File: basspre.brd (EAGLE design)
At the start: 37.5 x 28.7 mm, 26 parts, among them U101 TLE2426IDR, U102 LF351D, U103 LM4250

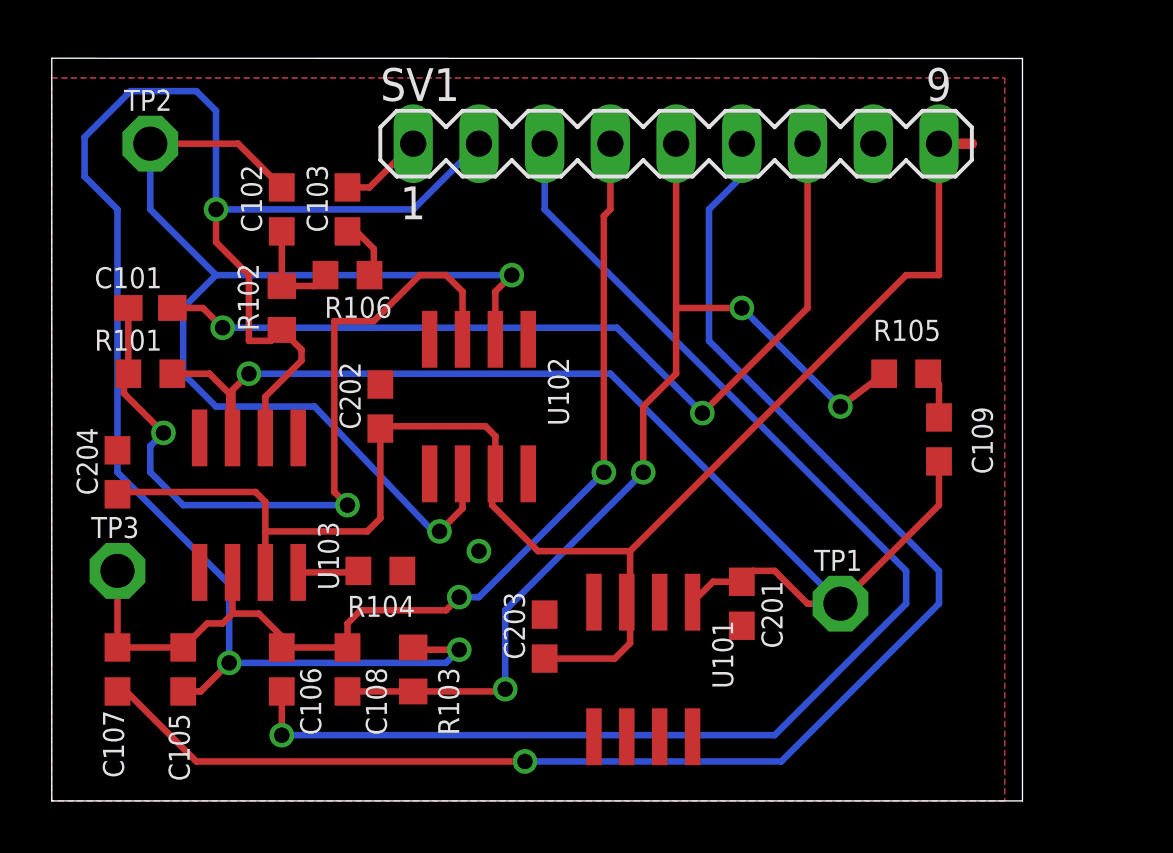
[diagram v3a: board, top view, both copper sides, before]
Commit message: switched to 10 pin system so bass pot can be three terminal in future revisions without changing connection.
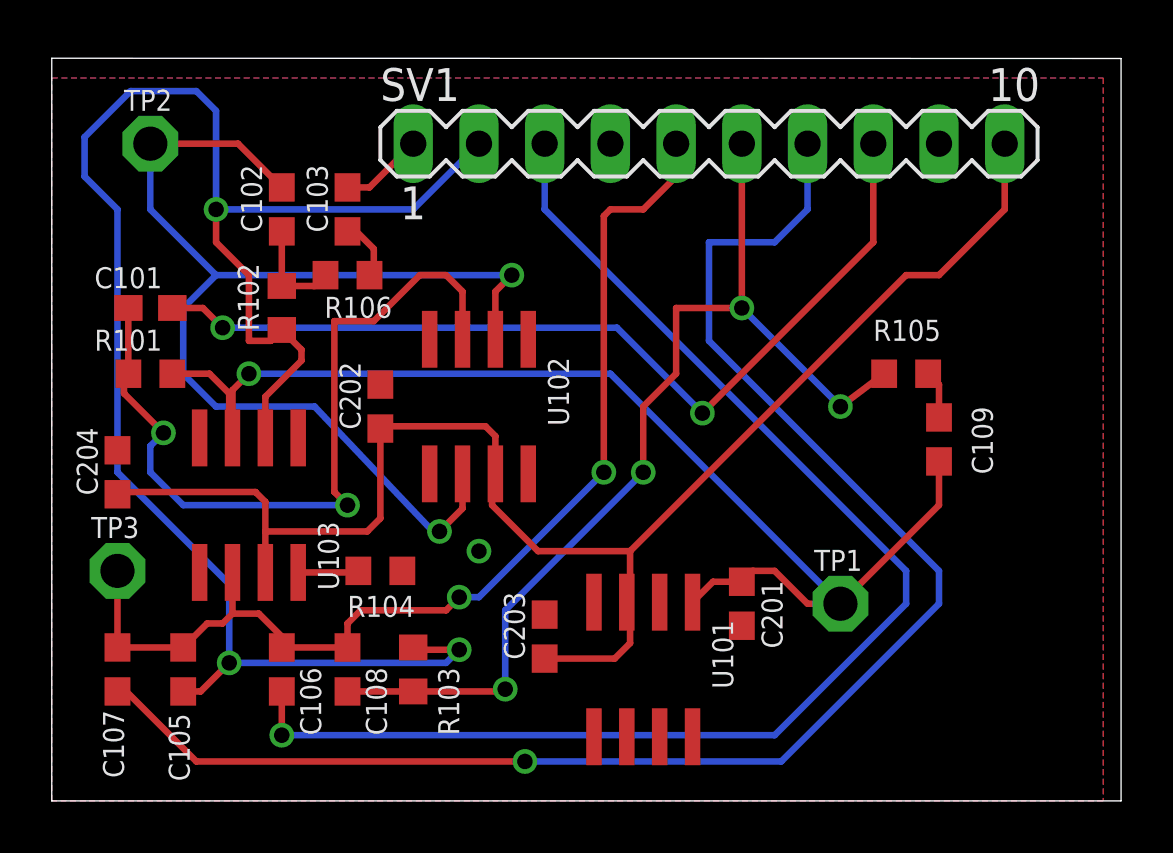
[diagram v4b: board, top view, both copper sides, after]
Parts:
- SV1: device con-lstb:MA09-1 -> con-lstb:MA10-1
- moved SV1 1.27 mm to (25.4, 25.4)
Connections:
- new net BASS3: SV1.4
- net BASS1: now also SV1.6; no longer SV1.5
- net BASS2: now also SV1.5; no longer SV1.4
- net GND: now also SV1.9; no longer SV1.8
- net INPUT: now also SV1.8; no longer SV1.7
- net OUTPUT: now also SV1.7; no longer SV1.6
- net V+: now also SV1.10; no longer SV1.9
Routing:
- net OUTPUT: track 57.4 -> 59.9 mm
- net BASS2: track 40.8 -> 42.6 mm
- net INPUT: track 34.3 -> 35.3 mm
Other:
- board size 37.5 x 28.7 mm -> 41.3 x 28.7 mm
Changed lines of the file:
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@@
 <board>
 <plain>
-<wire x1="0" y1="0" x2="37.516" y2="0" width="0" layer="20"/>
-<wire x1="37.516" y1="0" x2="37.516" y2="28.692" width="0" layer="20"/>
-<wire x1="37.516" y1="28.692" x2="0" y2="28.702" width="0" layer="20"/>
+<wire x1="0" y1="0" x2="41.326" y2="0" width="0" layer="20"/>
+<wire x1="41.326" y1="0" x2="41.326" y2="28.692" width="0" layer="20"/>
+<wire x1="41.326" y1="28.692" x2="0" y2="28.702" width="0" layer="20"/>
 <wire x1="0" y1="28.702" x2="0" y2="0" width="0" layer="20"/>
 <text x="35.56" y="17.78" size="1.6764" layer="22" font="vector" rot="MR0">BASSPRE-MM2
@@
 <attribute name="VALUE" x="4.572" y="11.811" size="1.27" layer="27" rot="R90"/>
 </element>
-<element name="SV1" library="con-lstb" package="MA09-1" value="" x="24.13" y="25.4">
-<attribute name="OC_NEWARK" value="unknown" x="49.53" y="8.89" size="1.778" layer="27" display="off"/>
-<attribute name="MPN" value="" x="49.53" y="8.89" size="1.778" layer="27" display="off"/>
-<attribute name="MF" value="" x="49.53" y="8.89" size="1.778" layer="27" display="off"/>
-<attribute name="OC_FARNELL" value="unknown" x="49.53" y="8.89" size="1.778" layer="27" display="off"/>
+<element name="SV1" library="con-lstb" package="MA10-1" value="" x="25.4" y="25.4">
+<attribute name="OC_NEWARK" value="unknown" x="50.8" y="8.89" size="1.778" layer="27" display="off"/>
+<attribute name="MPN" value="" x="50.8" y="8.89" size="1.778" layer="27" display="off"/>
+<attribute name="MF" value="" x="50.8" y="8.89" size="1.778" layer="27" display="off"/>
+<attribute name="OC_FARNELL" value="unknown" x="50.8" y="8.89" size="1.778" layer="27" display="off"/>
 </element>
 <element name="U$1" library="SparkFun" package="OSHW-LOGO-L" value="" x="32.766" y="12.7" rot="MR0"/>
@@
 <contactref element="U102" pad="4"/>
 <contactref element="U103" pad="4"/>
-<contactref element="SV1" pad="8"/>
 <contactref element="C204" pad="2"/>
 <contactref element="C201" pad="2"/>
@@
 <vertex x="0" y="0"/>
 <vertex x="0" y="27.94"/>
-<vertex x="36.83" y="27.94"/>
-<vertex x="36.83" y="0"/>
+<vertex x="40.64" y="27.94"/>
+<vertex x="40.64" y="0"/>
 </polygon>
 <polygon width="0.4064" layer="1">
 <vertex x="0" y="27.94"/>
-<vertex x="36.83" y="27.94"/>
-<vertex x="36.83" y="0"/>
+<vertex x="40.64" y="27.94"/>
+<vertex x="40.64" y="0"/>
 <vertex x="0" y="0"/>
 </polygon>
 <via x="16.51" y="9.652" extent="1-16" drill="0.6" shape="square"/>
+<contactref element="SV1" pad="9"/>
 </signal>
 <signal name="V+">
@@
 <contactref element="U103" pad="7"/>
 <contactref element="U102" pad="7"/>
-<contactref element="SV1" pad="9"/>
 <contactref element="C202" pad="1"/>
 <contactref element="C203" pad="1"/>
 <contactref element="C204" pad="1"/>
-<wire x1="34.29" y1="25.4" x2="35.56" y2="25.4" width="0.4064" layer="1"/>
-<wire x1="34.29" y1="25.4" x2="34.29" y2="20.32" width="0.254" layer="1"/>
 <wire x1="34.29" y1="20.32" x2="33.02" y2="20.32" width="0.254" layer="1"/>
 <wire x1="33.02" y1="20.32" x2="22.352" y2="9.652" width="0.254" layer="1"/>
@@
 <wire x1="12.7" y1="10.922" x2="12.192" y2="10.414" width="0.254" layer="1"/>
 <wire x1="12.192" y1="10.414" x2="8.255" y2="10.414" width="0.254" layer="1"/>
+<contactref element="SV1" pad="10"/>
+<wire x1="34.29" y1="20.32" x2="36.83" y2="22.86" width="0.254" layer="1"/>
+<wire x1="36.83" y1="22.86" x2="36.83" y2="25.4" width="0.254" layer="1"/>
 </signal>
 <signal name="N$2">
@@
 <signal name="INPUT">
 <contactref element="C101" pad="2"/>
-<contactref element="SV1" pad="7"/>
 <wire x1="4.66" y1="19.05" x2="5.842" y2="19.05" width="0.254" layer="1"/>
 <wire x1="5.842" y1="19.05" x2="6.604" y2="18.288" width="0.254" layer="1"/>
@@
 <wire x1="21.844" y1="18.288" x2="25.146" y2="14.986" width="0.254" layer="16"/>
 <via x="25.146" y="14.986" extent="1-16" drill="0.6" shape="square"/>
-<wire x1="25.146" y1="14.986" x2="29.21" y2="19.05" width="0.254" layer="1"/>
-<wire x1="29.21" y1="19.05" x2="29.21" y2="25.4" width="0.254" layer="1"/>
+<wire x1="25.146" y1="14.986" x2="31.75" y2="21.59" width="0.254" layer="1"/>
+<contactref element="SV1" pad="8"/>
+<wire x1="31.75" y1="21.59" x2="31.75" y2="25.4" width="0.254" layer="1"/>
 </signal>
 <signal name="BASS2">
@@
 <contactref element="C107" pad="2"/>
 <contactref element="TP3" pad="TP"/>
-<contactref element="SV1" pad="4"/>
 <wire x1="8.89" y1="5.93" x2="11.43" y2="5.93" width="0.254" layer="1"/>
 <wire x1="2.54" y1="5.93" x2="5.08" y2="5.93" width="0.254" layer="1"/>
@@
 <wire x1="21.336" y1="12.7" x2="21.336" y2="22.606" width="0.254" layer="1"/>
 <wire x1="21.336" y1="22.606" x2="21.59" y2="22.86" width="0.254" layer="1"/>
-<wire x1="21.59" y1="22.86" x2="21.59" y2="25.4" width="0.254" layer="1"/>
+<contactref element="SV1" pad="5"/>
+<wire x1="21.59" y1="22.86" x2="22.86" y2="22.86" width="0.254" layer="1"/>
+<wire x1="22.86" y1="22.86" x2="24.13" y2="24.13" width="0.254" layer="1"/>
+<wire x1="24.13" y1="24.13" x2="24.13" y2="25.4" width="0.254" layer="1"/>
 </signal>
 <signal name="TREBLE2">
@@
 <contactref element="R103" pad="2"/>
 <contactref element="C108" pad="2"/>
-<contactref element="SV1" pad="5"/>
 <wire x1="11.43" y1="4.23" x2="13.97" y2="4.23" width="0.254" layer="1"/>
 <wire x1="13.97" y1="4.23" x2="17.438" y2="4.23" width="0.254" layer="1"/>
@@
 <wire x1="24.13" y1="16.51" x2="24.13" y2="19.05" width="0.254" layer="1"/>
 <contactref element="R105" pad="1"/>
-<wire x1="24.13" y1="19.05" x2="24.13" y2="25.4" width="0.254" layer="1"/>
 <wire x1="32.17" y1="16.51" x2="30.48" y2="15.24" width="0.254" layer="1"/>
 <via x="30.48" y="15.24" extent="1-16" drill="0.6" shape="square"/>
@@
 <via x="26.67" y="19.05" extent="1-16" drill="0.6" shape="square"/>
 <wire x1="26.67" y1="19.05" x2="24.13" y2="19.05" width="0.254" layer="1"/>
+<contactref element="SV1" pad="6"/>
+<wire x1="26.67" y1="19.05" x2="26.67" y2="25.4" width="0.254" layer="1"/>
 </signal>
 <signal name="N$1">
@@
 </signal>
 <signal name="OUTPUT">
-<contactref element="SV1" pad="6"/>
 <contactref element="C107" pad="1"/>
 <wire x1="2.54" y1="4.23" x2="2.882" y2="4.23" width="0.254" layer="1"/>
@@
 <wire x1="34.29" y1="7.62" x2="34.29" y2="8.89" width="0.254" layer="16"/>
 <wire x1="34.29" y1="8.89" x2="25.4" y2="17.78" width="0.254" layer="16"/>
-<wire x1="25.4" y1="17.78" x2="25.4" y2="22.86" width="0.254" layer="16"/>
-<wire x1="25.4" y1="22.86" x2="26.67" y2="24.13" width="0.254" layer="16"/>
-<wire x1="26.67" y1="24.13" x2="26.67" y2="25.4" width="0.254" layer="16"/>
+<contactref element="SV1" pad="7"/>
+<wire x1="25.4" y1="17.78" x2="25.4" y2="21.59" width="0.254" layer="16"/>
+<wire x1="25.4" y1="21.59" x2="27.94" y2="21.59" width="0.254" layer="16"/>
+<wire x1="27.94" y1="21.59" x2="29.21" y2="22.86" width="0.254" layer="16"/>
+<wire x1="29.21" y1="22.86" x2="29.21" y2="25.4" width="0.254" layer="16"/>
 </signal>
 <signal name="N$4">
@@
 <wire x1="12.446" y1="20.486" x2="12.28" y2="20.32" width="0.254" layer="1"/>
 </signal>
+<signal name="BASS3">
+<contactref element="SV1" pad="4"/>
+</signal>
 </signals>

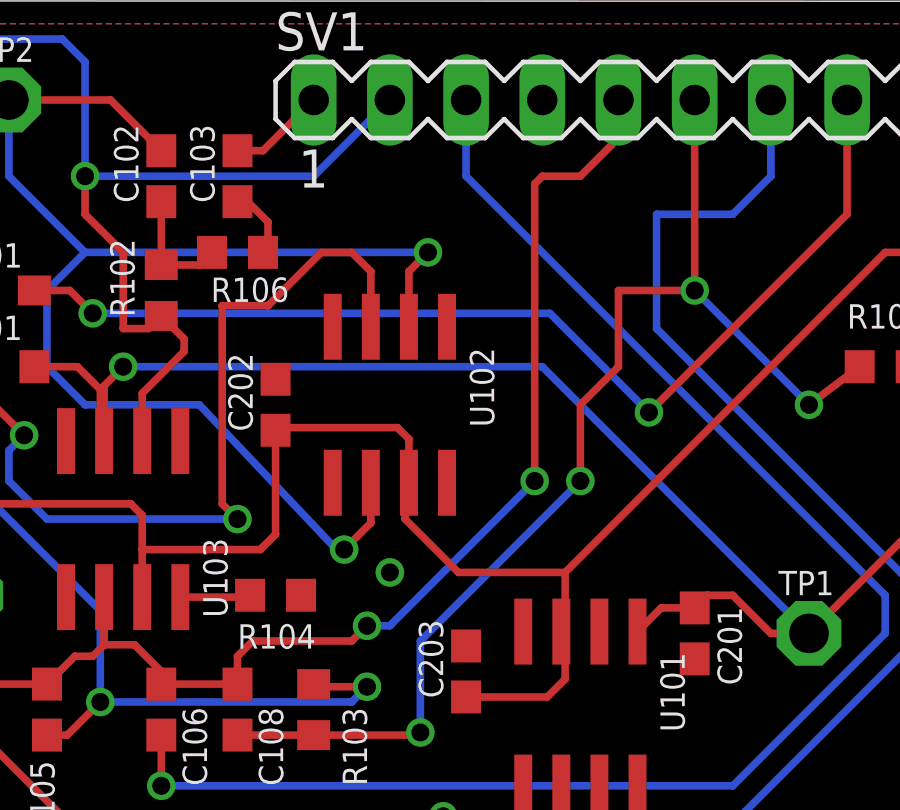
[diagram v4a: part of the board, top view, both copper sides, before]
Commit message: switched to two lm4250s for micropower operation, added readme
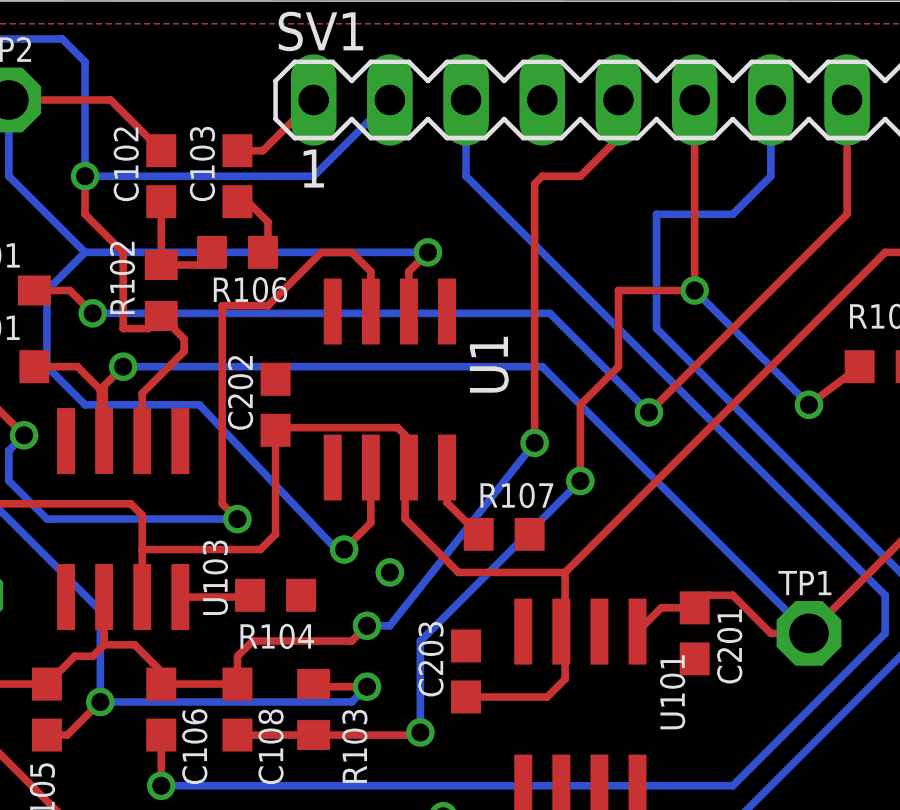
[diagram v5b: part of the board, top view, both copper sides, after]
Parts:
- removed U102: LF351D, linear:SO08
- added R107: 1.5M, resistor:R0603
- added U1: LM4250, russell_random:SOIC8
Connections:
- new net R107: R107.1, U1.8
- net C1: now also U1.3; no longer U102.3
- net GND: now also R107.2, U1.4; no longer U102.4
- net N$3: now also U1.2, U1.6; no longer U102.2, U102.6
- net V+: now also U1.7; no longer U102.7
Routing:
- net R107: track 0.00 -> 2.66 mm
- net C1: track 30.5 -> 30.0 mm
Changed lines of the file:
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@@
 <attribute name="VALUE" x="11.811" y="6.858" size="1.27" layer="27"/>
-</element>
-<element name="U102" library="linear" package="SO08" value="LF351D" x="16.51" y="15.24" smashed="yes" rot="R180">
-<attribute name="NAME" x="19.177" y="17.145" size="0.8128" layer="25" rot="R270"/>
-<attribute name="VALUE" x="12.573" y="17.145" size="1.27" layer="27" rot="R270"/>
 </element>
 <element name="C101" library="resistor" package="C0603" value="1uF" x="3.81" y="19.05" smashed="yes">
@@
 <attribute name="VALUE" x="10.541" y="18.288" size="1.27" layer="27"/>
 </element>
+<element name="U1" library="russell_random" package="SOIC8" value="LM4250" x="16.51" y="15.748" rot="R180"/>
+<element name="R107" library="resistor" package="R0603" value="1.5M" x="20.32" y="10.922" smashed="yes">
+<attribute name="NAME" x="19.431" y="11.811" size="0.8128" layer="25"/>
+<attribute name="VALUE" x="19.431" y="8.89" size="1.27" layer="27"/>
+</element>
 </elements>
 <signals>
@@
 <contactref element="U101" pad="2"/>
 <contactref element="R104" pad="2"/>
-<contactref element="U102" pad="4"/>
 <contactref element="U103" pad="4"/>
 <contactref element="C204" pad="2"/>
@@
 <via x="16.51" y="9.652" extent="1-16" drill="0.6" shape="square"/>
 <contactref element="SV1" pad="9"/>
+<contactref element="U1" pad="4"/>
+<contactref element="R107" pad="2"/>
 </signal>
 <signal name="V+">
 <contactref element="U101" pad="3"/>
 <contactref element="U103" pad="7"/>
-<contactref element="U102" pad="7"/>
 <contactref element="C202" pad="1"/>
 <contactref element="C203" pad="1"/>
@@
 <wire x1="22.352" y1="9.652" x2="18.796" y2="9.652" width="0.254" layer="1"/>
 <wire x1="18.796" y1="9.652" x2="17.018" y2="11.43" width="0.254" layer="1"/>
-<wire x1="17.018" y1="11.43" x2="17.018" y2="12.513" width="0.254" layer="1"/>
-<wire x1="17.018" y1="12.513" x2="17.145" y2="12.64" width="0.254" layer="1"/>
-<wire x1="17.145" y1="12.64" x2="17.145" y2="14.097" width="0.254" layer="1"/>
+<wire x1="17.018" y1="11.43" x2="17.018" y2="13.148" width="0.254" layer="1"/>
 <wire x1="17.145" y1="14.097" x2="16.764" y2="14.478" width="0.254" layer="1"/>
 <wire x1="16.764" y1="14.478" x2="12.788" y2="14.478" width="0.254" layer="1"/>
@@
 <wire x1="34.29" y1="20.32" x2="36.83" y2="22.86" width="0.254" layer="1"/>
 <wire x1="36.83" y1="22.86" x2="36.83" y2="25.4" width="0.254" layer="1"/>
+<contactref element="U1" pad="7"/>
+<wire x1="17.145" y1="14.097" x2="17.145" y2="13.148" width="0.254" layer="1"/>
+<wire x1="17.145" y1="13.148" x2="17.018" y2="13.148" width="0.254" layer="1"/>
 </signal>
 <signal name="N$2">
@@
 </signal>
 <signal name="N$3">
-<contactref element="U102" pad="2"/>
-<contactref element="U102" pad="6"/>
 <contactref element="C102" pad="2"/>
 <contactref element="TP2" pad="TP"/>
 <wire x1="3.81" y1="25.4" x2="7.2" y2="25.4" width="0.254" layer="1"/>
 <wire x1="7.2" y1="25.4" x2="8.89" y2="23.71" width="0.254" layer="1"/>
-<wire x1="17.145" y1="17.84" x2="17.145" y2="19.685" width="0.254" layer="1"/>
 <wire x1="17.145" y1="19.685" x2="17.78" y2="20.32" width="0.254" layer="1"/>
 <via x="17.78" y="20.32" extent="1-16" drill="0.6" shape="square"/>
@@
 <wire x1="6.35" y1="20.32" x2="3.81" y2="22.86" width="0.254" layer="16"/>
 <wire x1="3.81" y1="22.86" x2="3.81" y2="25.4" width="0.254" layer="16"/>
-<wire x1="15.875" y1="12.64" x2="15.875" y2="11.303" width="0.254" layer="1"/>
 <wire x1="15.875" y1="11.303" x2="14.986" y2="10.414" width="0.254" layer="1"/>
 <via x="14.986" y="10.414" extent="1-16" drill="0.6" shape="square"/>
@@
 <wire x1="5.08" y1="16.51" x2="5.08" y2="19.05" width="0.254" layer="16"/>
 <wire x1="5.08" y1="19.05" x2="6.35" y2="20.32" width="0.254" layer="16"/>
+<contactref element="U1" pad="2"/>
+<contactref element="U1" pad="6"/>
+<wire x1="17.145" y1="18.348" x2="17.145" y2="19.685" width="0.254" layer="1"/>
+<wire x1="15.875" y1="13.148" x2="15.875" y2="11.303" width="0.254" layer="1"/>
 </signal>
 <signal name="C1">
-<contactref element="U102" pad="3"/>
 <contactref element="C101" pad="1"/>
 <contactref element="R101" pad="1"/>
 <wire x1="2.96" y1="19.05" x2="2.96" y2="16.51" width="0.254" layer="1"/>
-<wire x1="15.875" y1="17.84" x2="15.875" y2="19.685" width="0.254" layer="1"/>
 <wire x1="15.875" y1="19.685" x2="15.24" y2="20.32" width="0.254" layer="1"/>
 <wire x1="10.922" y1="18.542" x2="10.922" y2="11.938" width="0.254" layer="1"/>
@@
 <wire x1="12.446" y1="18.542" x2="14.224" y2="20.32" width="0.254" layer="1"/>
 <wire x1="14.224" y1="20.32" x2="15.24" y2="20.32" width="0.254" layer="1"/>
+<contactref element="U1" pad="3"/>
+<wire x1="15.875" y1="19.685" x2="15.875" y2="18.348" width="0.254" layer="1"/>
 </signal>
 <signal name="INPUT">
@@
 <via x="15.748" y="7.874" extent="1-16" drill="0.6" shape="square"/>
 <wire x1="15.748" y1="7.874" x2="16.51" y2="7.874" width="0.254" layer="16"/>
-<wire x1="16.51" y1="7.874" x2="21.336" y2="12.7" width="0.254" layer="16"/>
-<via x="21.336" y="12.7" extent="1-16" drill="0.6" shape="square"/>
-<wire x1="21.336" y1="12.7" x2="21.336" y2="22.606" width="0.254" layer="1"/>
+<wire x1="16.51" y1="7.874" x2="21.336" y2="13.97" width="0.254" layer="16"/>
+<via x="21.336" y="13.97" extent="1-16" drill="0.6" shape="square"/>
+<wire x1="21.336" y1="13.97" x2="21.336" y2="22.606" width="0.254" layer="1"/>
 <wire x1="21.336" y1="22.606" x2="21.59" y2="22.86" width="0.254" layer="1"/>
 <contactref element="SV1" pad="5"/>
@@
 <contactref element="SV1" pad="4"/>
 </signal>
+<signal name="R107">
+<contactref element="U1" pad="8"/>
+<contactref element="R107" pad="1"/>
+<wire x1="18.415" y1="13.148" x2="18.415" y2="11.977" width="0.254" layer="1"/>
+<wire x1="18.415" y1="11.977" x2="19.47" y2="10.922" width="0.254" layer="1"/>
+</signal>
 </signals>
